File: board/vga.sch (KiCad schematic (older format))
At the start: 34 parts, among them P601 3-RCA

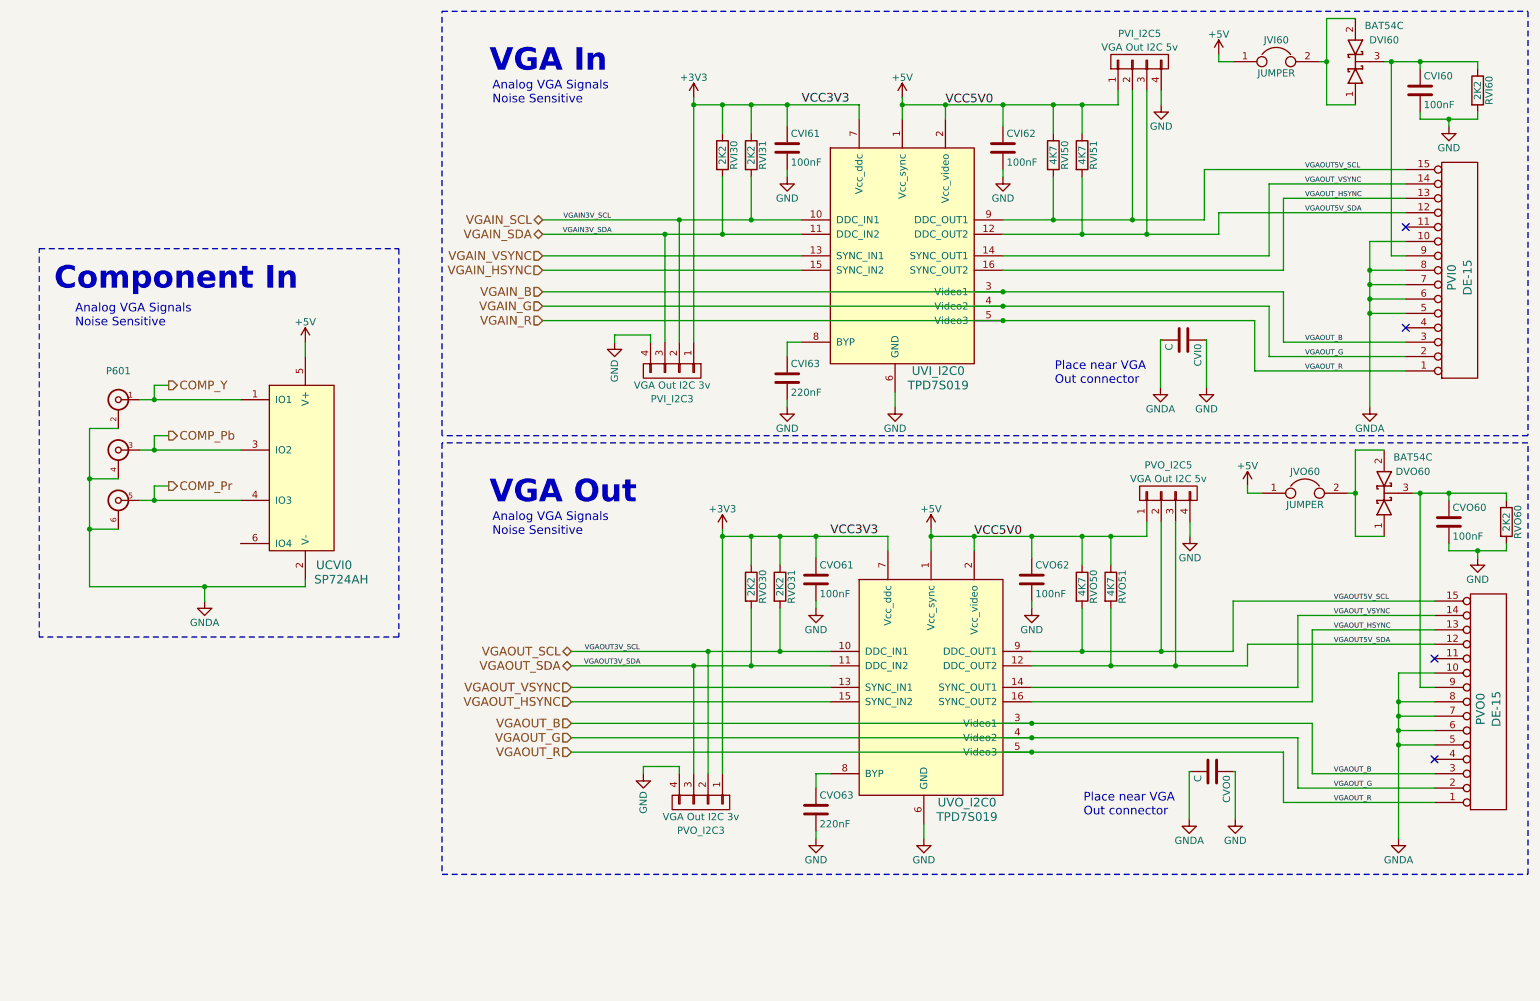
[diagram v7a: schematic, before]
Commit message: Small cleanups.
 * Move TPD7S019 and SP724AH into their own library.
 * Use 2 x 100nF capacitors for TPD7S019 bypass (save a part line).
 * Adding a couple of notes.
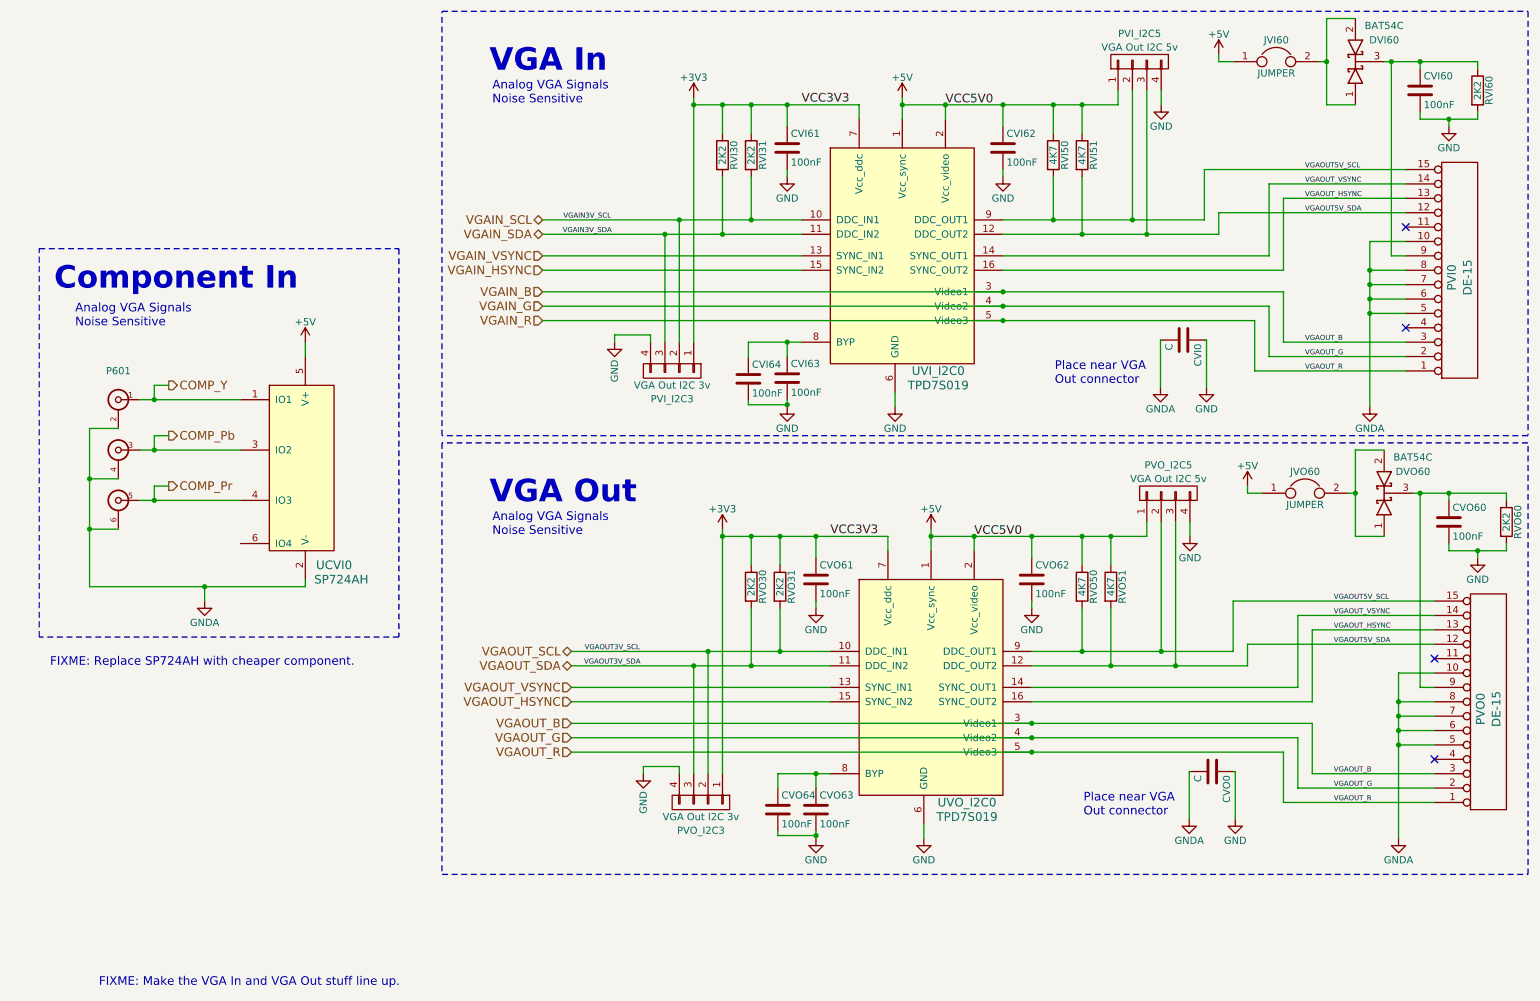
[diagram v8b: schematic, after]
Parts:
- added CVI64, CVO64: 100nF, symbol C
- CVI63, CVO63: value 220nF -> 100nF
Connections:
- net GND: now also CVI64.2, CVO64.2
- net at CVO63.1, UVO_I2C0.8 (BYP): now also CVO64.1
- net at CVI63.1, UVI_I2C0.8 (BYP): now also CVI64.1
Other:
- note added: "FIXME: Make the VGA In and VGA Out stuff line up."
- note added: "FIXME: Replace SP724AH with cheaper component."
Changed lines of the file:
@@
 LIBS:ad9984-power
 LIBS:3-rca
+LIBS:SP724AH
+LIBS:TPD7S019
 EELAYER 25 0
 EELAYER END
@@
 P 6100 6050
 F 0 "CVO63" H 6125 6150 50  0000 L CNN
-F 1 "220nF" H 6125 5950 50  0000 L CNN
+F 1 "100nF" H 6125 5950 50  0000 L CNN
 F 2 "" H 6138 5900 50  0000 C CNN
 F 3 "" H 6100 6050 50  0000 C CNN
@@
 	6100 6250 6100 6200
 Wire Wire Line
-	6200 5800 6100 5800
+	5835 5800 6200 5800
 Wire Wire Line
 	6100 5800 6100 5900
@@
 P 5900 3050
 F 0 "CVI63" H 5925 3150 50  0000 L CNN
-F 1 "220nF" H 5925 2950 50  0000 L CNN
+F 1 "100nF" H 5925 2950 50  0000 L CNN
 F 2 "" H 5938 2900 50  0000 C CNN
 F 3 "" H 5900 3050 50  0000 C CNN
@@
 	5900 3250 5900 3200
 Wire Wire Line
-	6000 2800 5900 2800
+	5630 2800 6000 2800
 Wire Wire Line
 	5900 2800 5900 2900
@@
 Wire Notes Line
 	700  4850 700  2150
+$Comp
+L C CVO64
+U 1 1 57ABE0F6
+P 5835 6050
+F 0 "CVO64" H 5860 6150 50  0000 L CNN
+F 1 "100nF" H 5860 5950 50  0000 L CNN
+F 2 "" H 5873 5900 50  0000 C CNN
+F 3 "" H 5835 6050 50  0000 C CNN
+	1    5835 6050
+	1    0    0    -1
+$EndComp
+Wire Wire Line
+	5835 5800 5835 5900
+Connection ~ 6100 5800
+Wire Wire Line
+	5835 6200 5835 6230
+Wire Wire Line
+	5835 6230 6100 6230
+Connection ~ 6100 6230
+$Comp
+L C CVI64
+U 1 1 57ABE940
+P 5630 3055
+F 0 "CVI64" H 5655 3155 50  0000 L CNN
+F 1 "100nF" H 5655 2955 50  0000 L CNN
+F 2 "" H 5668 2905 50  0000 C CNN
+F 3 "" H 5630 3055 50  0000 C CNN
+	1    5630 3055
+	1    0    0    -1
+$EndComp
+Wire Wire Line
+	5630 2905 5630 2800
+Connection ~ 5900 2800
+Wire Wire Line
+	5900 3235 5630 3235
+Wire Wire Line
+	5630 3235 5630 3205
+Connection ~ 5900 3235
+Text Notes 1115 7285 0    60   ~ 0
+FIXME: Make the VGA In and VGA Out stuff line up.
+Text Notes 775  5060 0    60   ~ 0
+FIXME: Replace SP724AH with cheaper component.
 $EndSCHEMATC
